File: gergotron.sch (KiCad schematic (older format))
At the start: 32 parts, among them CON1 ER-OLED-FPC30, J1 KMDGX-6S-BS, J2 KMDGX-6S-BS, J3 AudioJack3_TRS_TN, P1 Power, P2 Analog, P3 Digital, P4 Digital, P5 CONN_01X01, P6 CONN_01X01, P7 CONN_01X01, P8 CONN_01X01, U1 TXB0104D, U2 PCM1808PWG4

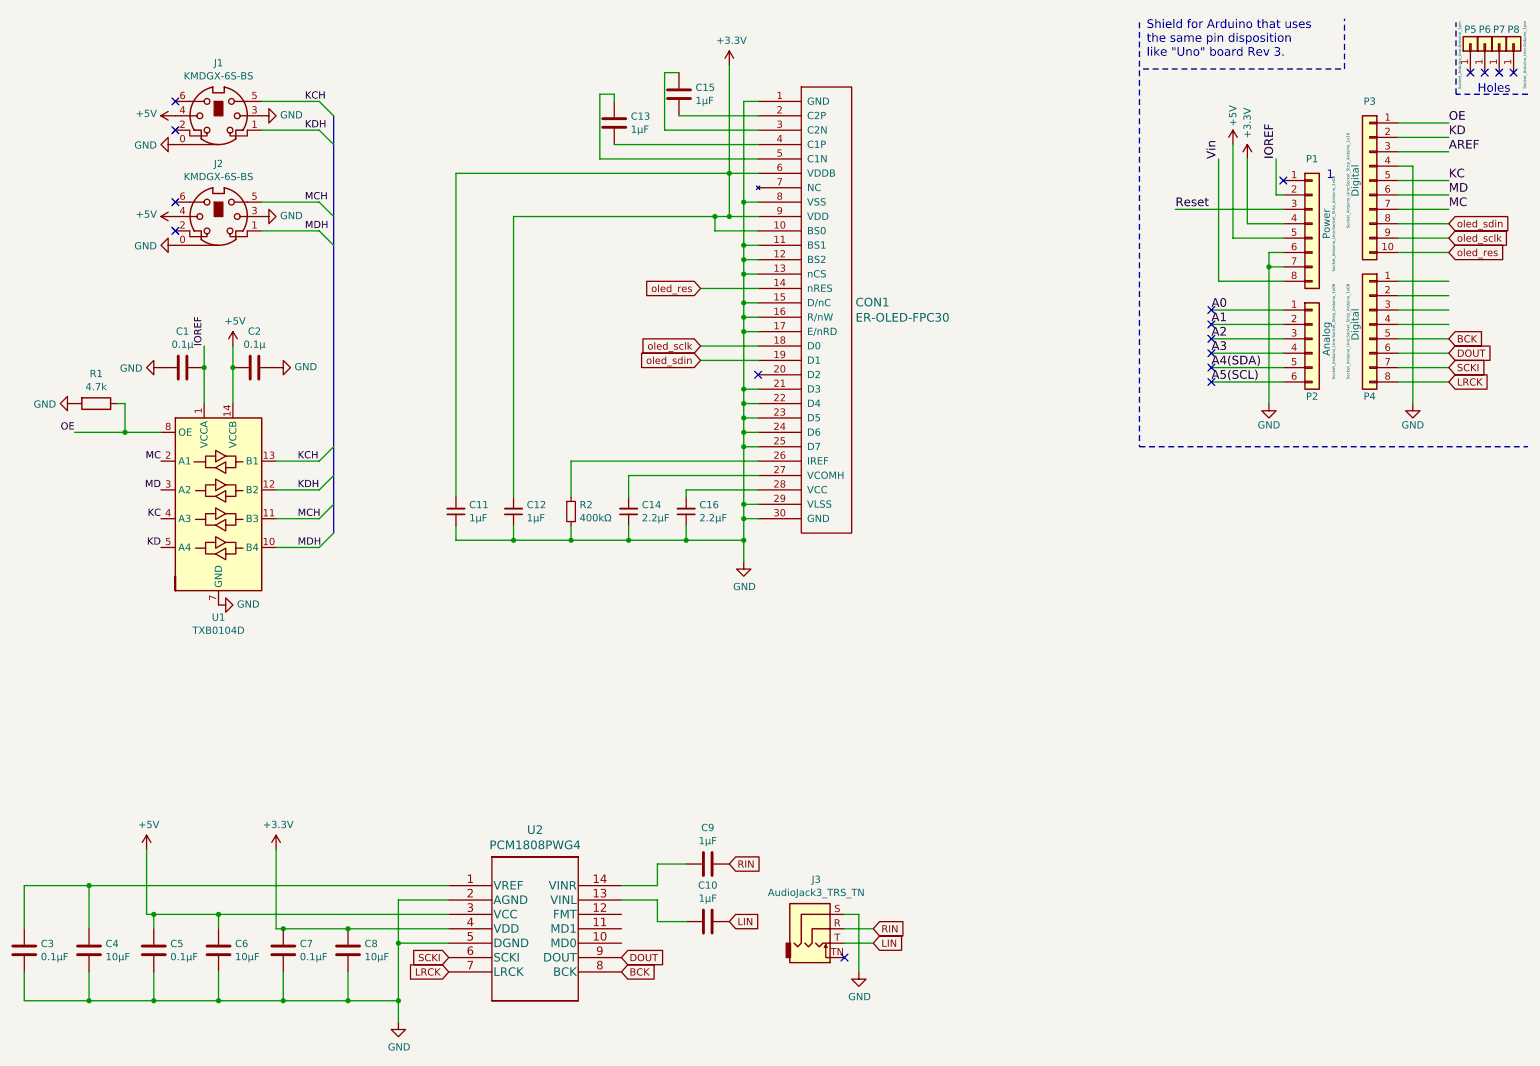
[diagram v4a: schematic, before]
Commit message: Start work on the DAC
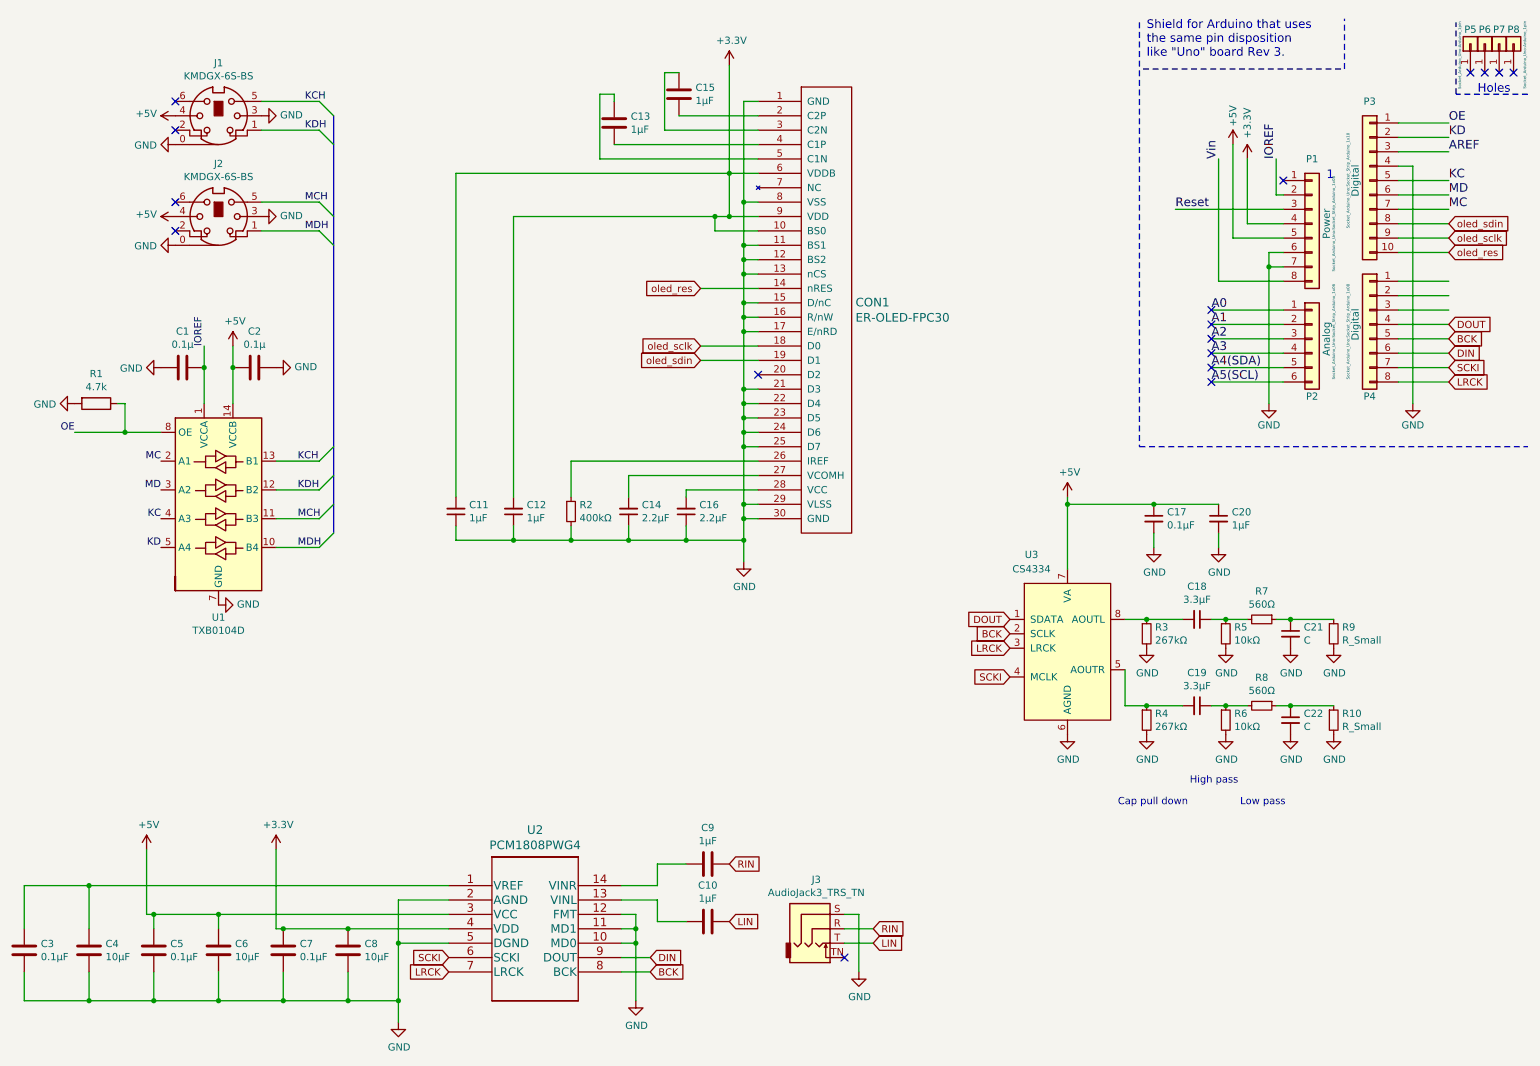
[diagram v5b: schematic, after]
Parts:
- added C17: 0.1μF, Capacitor_SMD:C_0603_1608Metric, symbol Device:C_Small
- added C18, C19: 3.3μF, Capacitor_SMD:C_0603_1608Metric, symbol Device:C_Small
- added C20: 1μF, Capacitor_SMD:C_0603_1608Metric, symbol Device:C_Small
- added C21, C22: C, Capacitor_SMD:C_0603_1608Metric, symbol Device:C_Small
- added R10, R9: R_Small, Resistor_SMD:R_0603_1608Metric, symbol Device:R_Small
- added R3, R4: 267kΩ, Resistor_SMD:R_0603_1608Metric, symbol Device:R_Small
- added R5, R6: 10kΩ, Resistor_SMD:R_0603_1608Metric, symbol Device:R_Small
- added R7, R8: 560Ω, Resistor_SMD:R_0603_1608Metric, symbol Device:R_Small
- added U3: CS4334, Package_SO:SOIC-8_3.9x4.9mm_P1.27mm, symbol CS4334:CS4334
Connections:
- net +5V: now also C17.1, C20.1, U3.7 (VA)
- net BCK: now also U3.2 (SCLK)
- net DOUT: now also P4.4 (Pin_4), U3.1 (SDATA); no longer P4.6 (Pin_6), U2.9 (DOUT)
- net GND: now also U2.10 (MD0), U2.11 (MD1), U2.12 (FMT), C17.2, C20.2, C21.2, C22.2, R10.2, R3.2, R4.2, R5.2, R6.2, R9.2, U3.6 (AGND)
- net LRCK: now also U3.3 (LRCK)
- net SCKI: now also U3.4 (MCLK)
- new net: C19.2, R4.1, U3.5 (AOUTR)
- new net: C18.2, R3.1, U3.8 (AOUTL)
- new net: C19.1, R6.1, R8.2
- new net: C22.1, R10.1, R8.1
- new net: C18.1, R5.1, R7.2
- new net: C21.1, R7.1, R9.1
- new net DIN: P4.6 (Pin_6), U2.9 (DOUT)
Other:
- note added: "Cap pull down"
- note added: "High pass"
- note added: "Low pass"

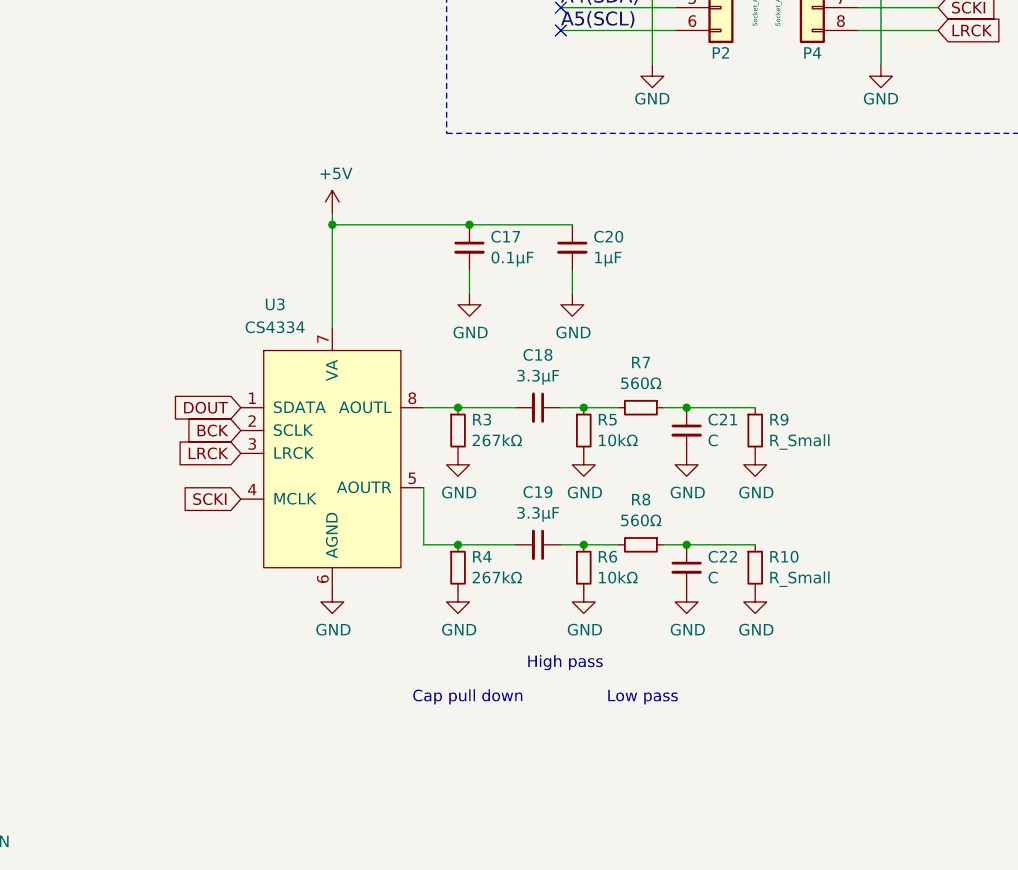
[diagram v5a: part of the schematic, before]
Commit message: remove audio out
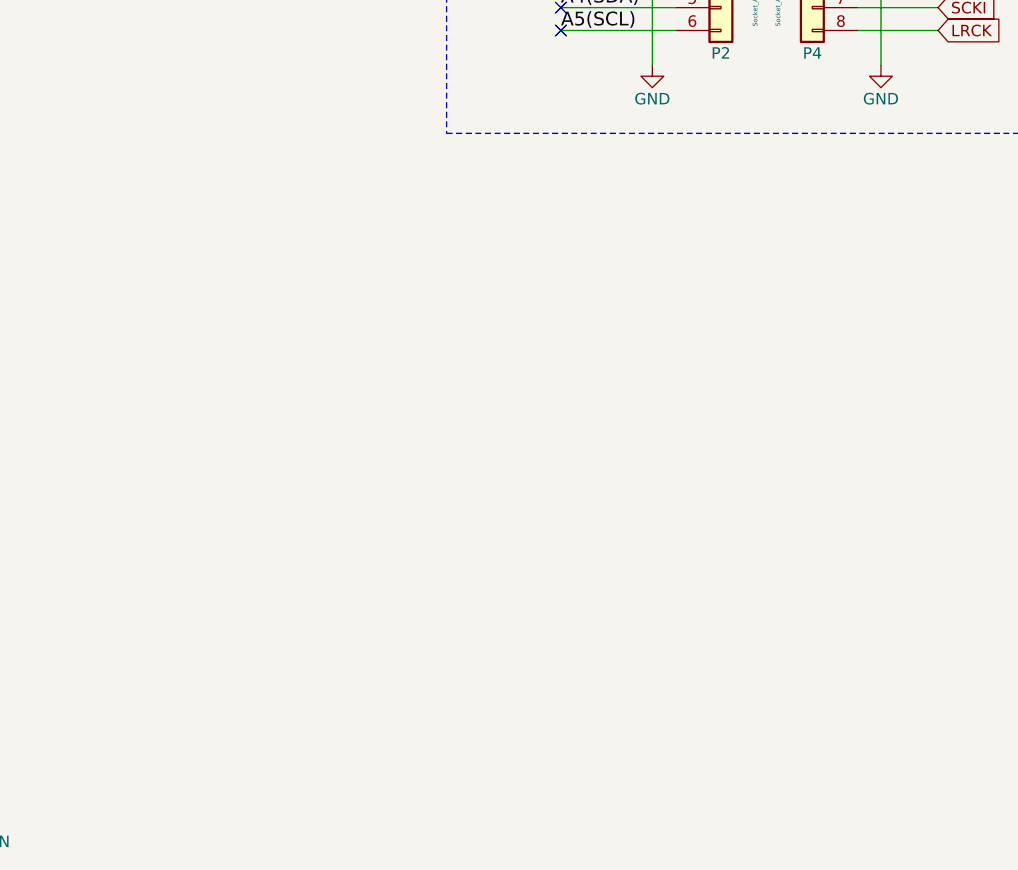
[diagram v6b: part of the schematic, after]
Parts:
- removed C17: 0.1μF, Capacitor_SMD:C_0603_1608Metric, symbol Device:C_Small
- removed C18, C19: 3.3μF, Capacitor_SMD:C_0603_1608Metric, symbol Device:C_Small
- removed C20: 1μF, Capacitor_SMD:C_0603_1608Metric, symbol Device:C_Small
- removed C21, C22: C, Capacitor_SMD:C_0603_1608Metric, symbol Device:C_Small
- removed R10, R9: R_Small, Resistor_SMD:R_0603_1608Metric, symbol Device:R_Small
- removed R3, R4: 267kΩ, Resistor_SMD:R_0603_1608Metric, symbol Device:R_Small
- removed R5, R6: 10kΩ, Resistor_SMD:R_0603_1608Metric, symbol Device:R_Small
- removed R7, R8: 560Ω, Resistor_SMD:R_0603_1608Metric, symbol Device:R_Small
- removed U3: CS4334, Package_SO:SOIC-8_3.9x4.9mm_P1.27mm, symbol CS4334:CS4334
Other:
- note removed: "Cap pull down"
- note removed: "High pass"
- note removed: "Low pass"
